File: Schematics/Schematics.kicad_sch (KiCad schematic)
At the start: 14 parts, among them U1 XIAO ESP32C3, U2 TP4056-42-ESOP8

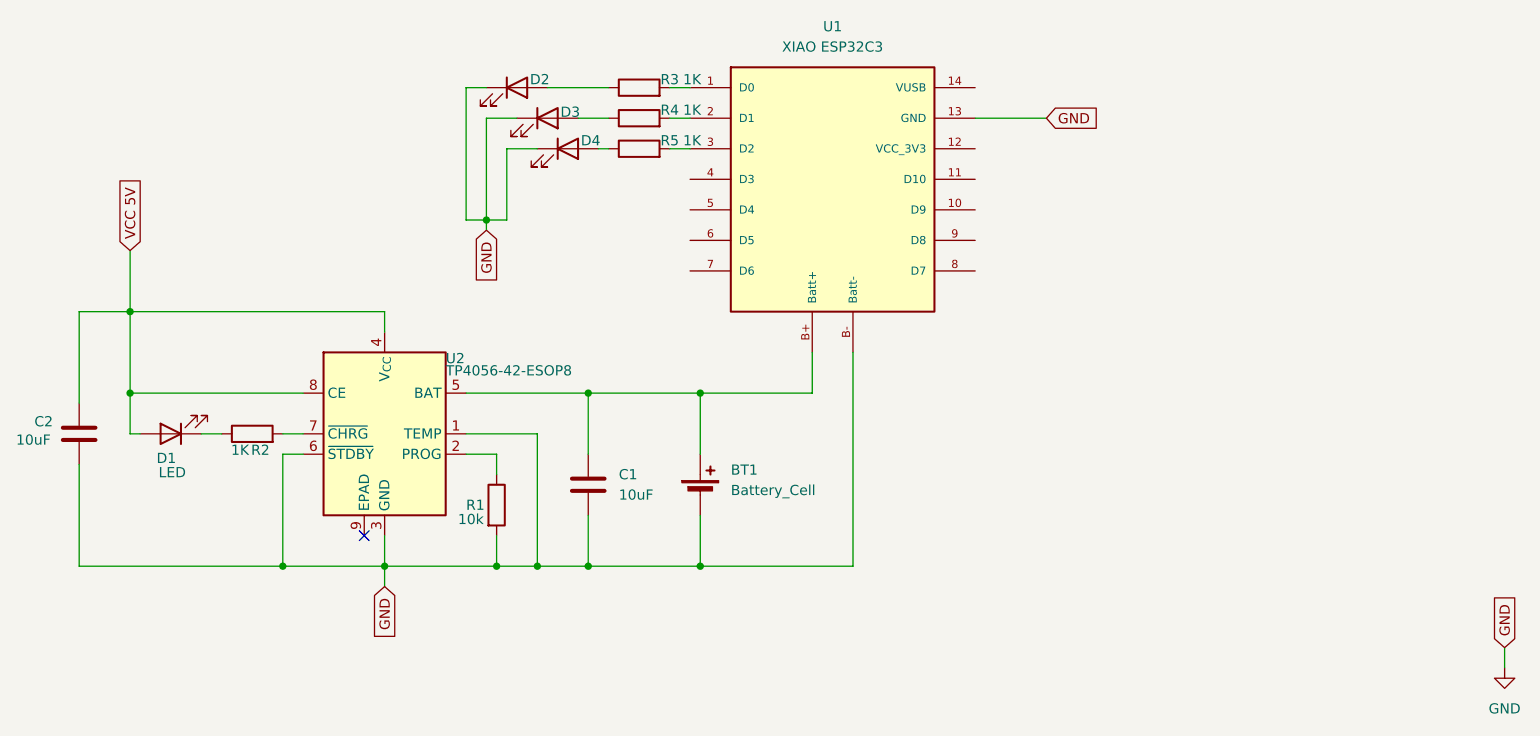
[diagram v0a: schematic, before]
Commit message: removed external charge module as it is already included
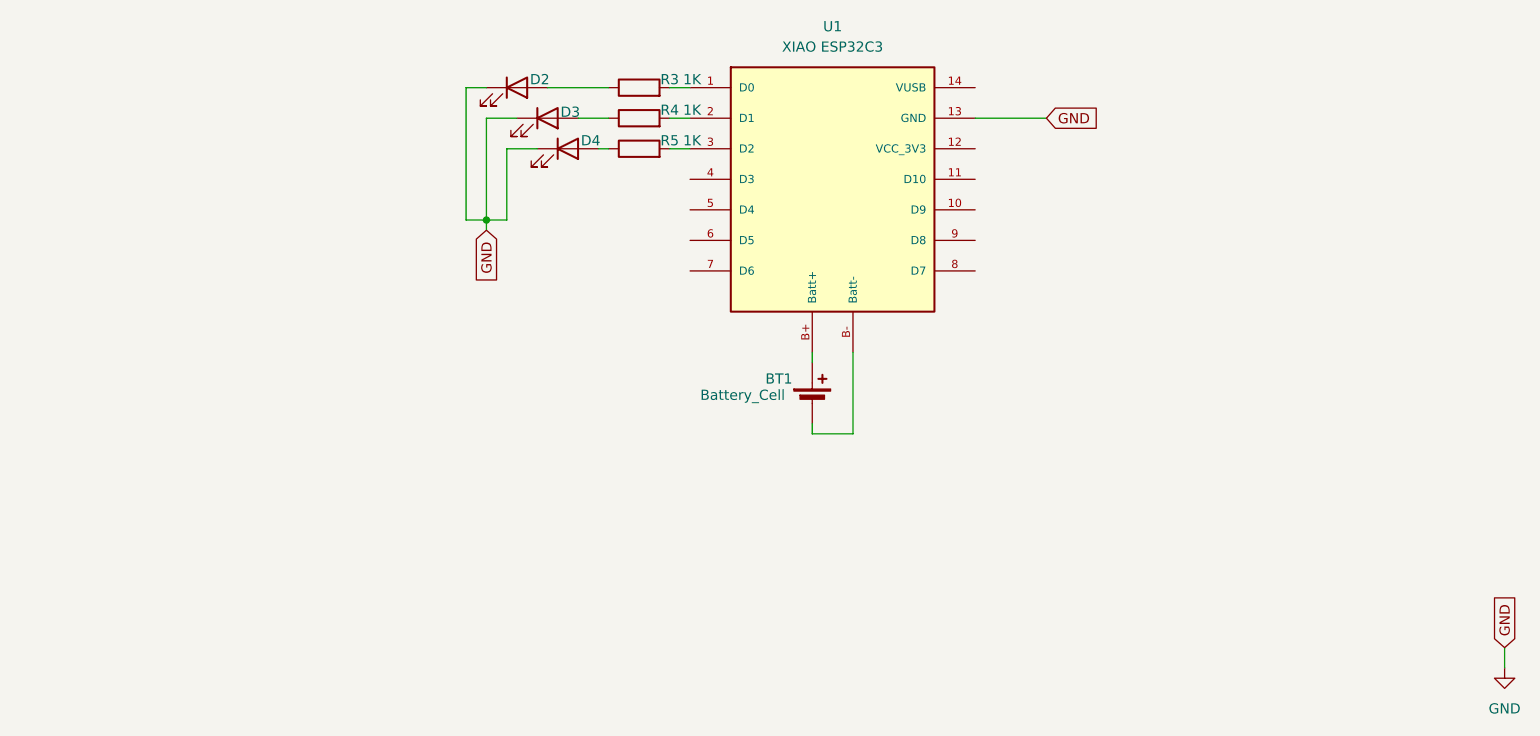
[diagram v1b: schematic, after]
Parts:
- removed C1, C2: 10uF, Capacitor_SMD:C_0603_1608Metric, symbol Device:C
- removed D1: LED, LED_SMD:LED_0603_1608Metric, symbol Device:LED
- removed R1: 10k, Resistor_SMD:R_0603_1608Metric, symbol Device:R
- removed R2: 1K, Resistor_SMD:R_0603_1608Metric, symbol Device:R
- removed U2: TP4056-42-ESOP8, Package_SO:SOIC-8-1EP_3.9x4.9mm_P1.27mm_EP2.41x3.3mm_ThermalVias, symbol Battery_Management:TP4056-42-ESOP8
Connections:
- net GND: no longer BT1.2 (-), U1.B- (Batt-)
- new net: BT1.2 (-), U1.B- (Batt-)
- no-connect marks 1 -> 0
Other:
- moved on the sheet: BT1

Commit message: redesign of the display and LEDs
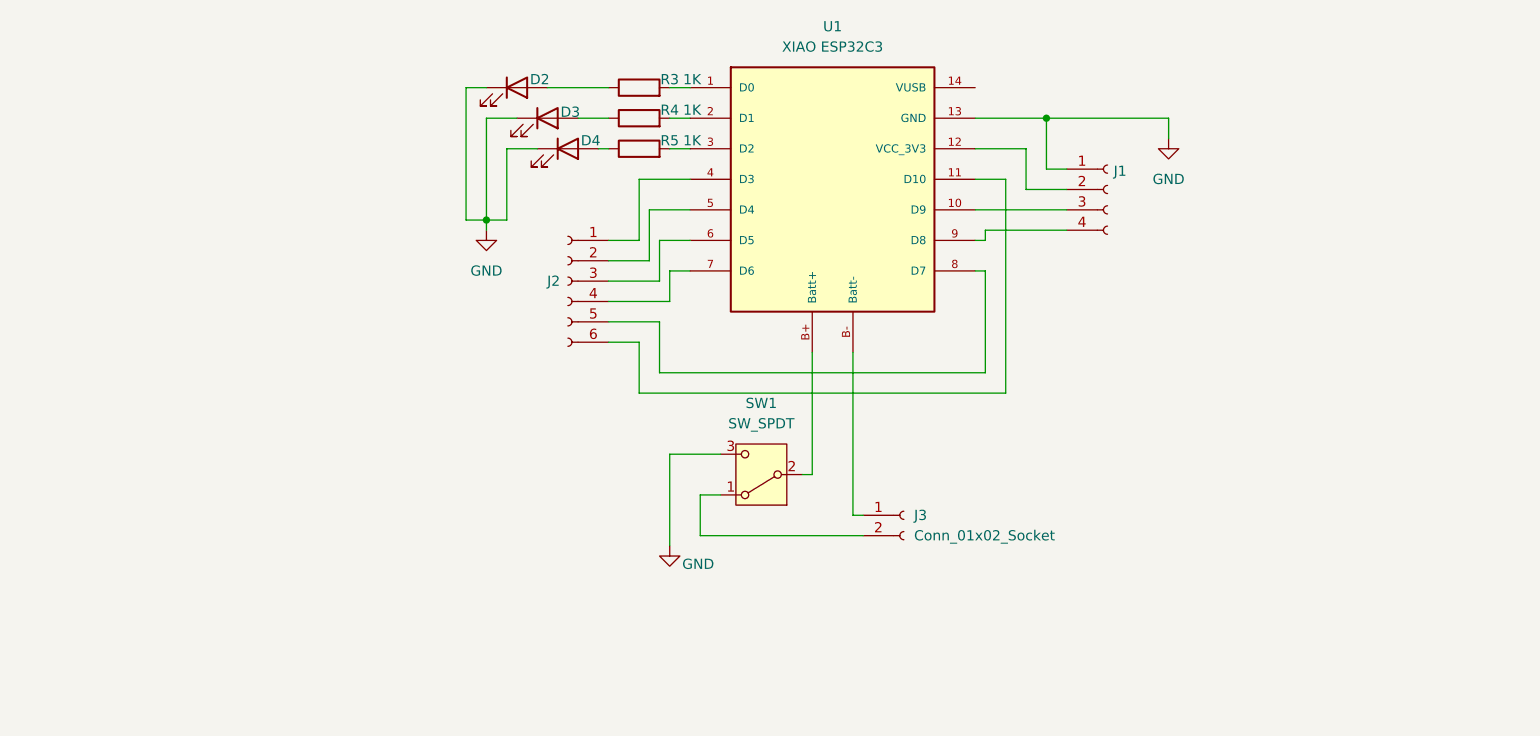
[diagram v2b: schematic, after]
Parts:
- removed BT1: Battery_Cell, Battery:BatteryHolder_MPD_BH-18650-PC, symbol Device:Battery_Cell
- added J1: Conn_01x04_Socket, Connector_PinSocket_2.54mm:PinSocket_1x04_P2.54mm_Vertical, symbol Connector:Conn_01x04_Socket
- added J2: Conn_01x06_Socket, Connector_PinSocket_2.54mm:PinSocket_1x06_P2.54mm_Vertical, symbol Connector:Conn_01x06_Socket
- added J3: Conn_01x02_Socket, Connector_PinSocket_2.54mm:PinSocket_1x02_P2.54mm_Vertical, symbol Connector:Conn_01x02_Socket
- added SW1: SW_SPDT, Button_Switch_SMD:SW_SPDT_PCM12, symbol Switch:SW_SPDT
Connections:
- net GND: now also J1.1 (Pin_1), SW1.3 (C)
- net at U1.B+ (Batt+): now also SW1.2 (B)
- net at U1.B- (Batt-): now also J3.1 (Pin_1)
- net at U1.10 (D9): now also J1.3 (Pin_3)
- net at U1.11 (D10): now also J2.6 (Pin_6)
- net at U1.12 (VCC_3V3): now also J1.2 (Pin_2)
- net at U1.4 (D3): now also J2.1 (Pin_1)
- net at U1.5 (D4): now also J2.2 (Pin_2)
- net at U1.6 (D5): now also J2.3 (Pin_3)
- net at U1.7 (D6): now also J2.4 (Pin_4)
- net at U1.8 (D7): now also J2.5 (Pin_5)
- net at U1.9 (D8): now also J1.4 (Pin_4)
- new net: J3.2 (Pin_2), SW1.1 (A)
